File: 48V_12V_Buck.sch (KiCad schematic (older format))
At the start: 63 parts, among them Q4 CSD18534Q5A, Q5 CSD18540Q5B

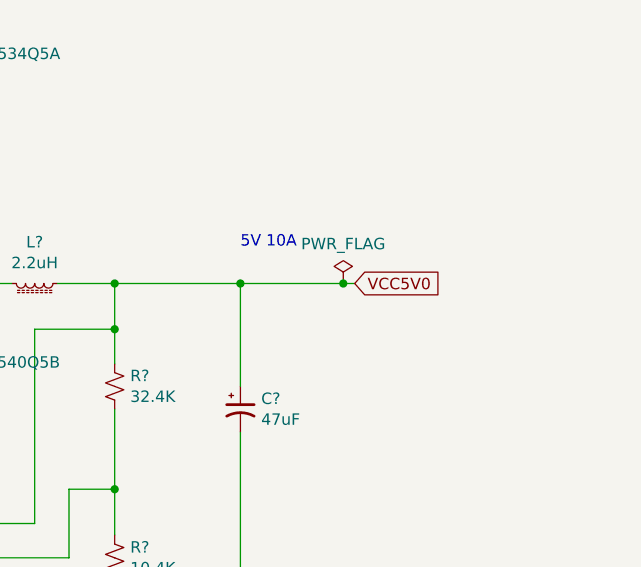
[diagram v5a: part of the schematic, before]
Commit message: Added USB3 type B connector Added ESD protection to the same sheet
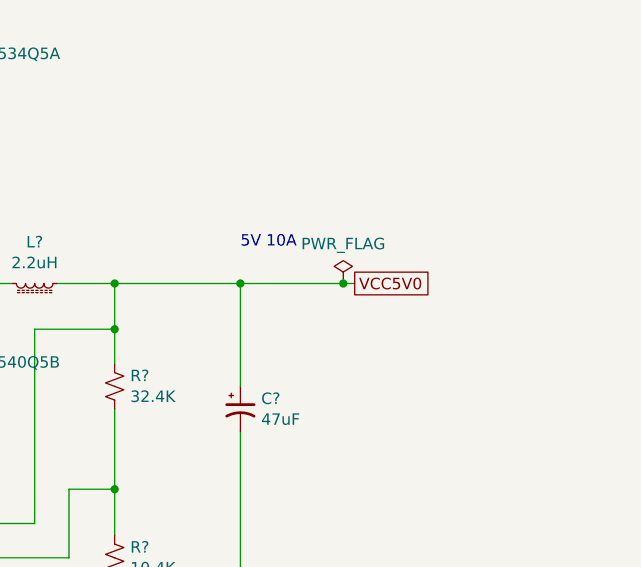
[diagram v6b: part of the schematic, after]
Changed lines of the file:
@@
 Text Notes 9050 8525 0    50   ~ 0
 5V 10A
-Text GLabel 9550 8675 2    50   Input ~ 0
+Text GLabel 9550 8675 2    50   UnSpc ~ 0
 VCC5V0
 $Comp
